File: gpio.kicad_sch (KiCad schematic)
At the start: 5 parts, among them J1 CONN_02X20, J2 CONN_02X20

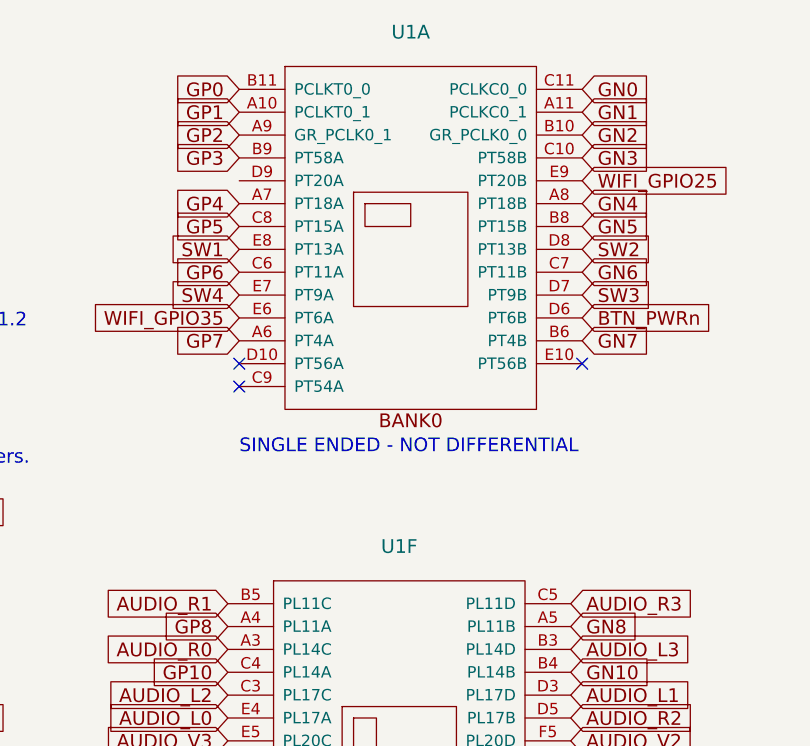
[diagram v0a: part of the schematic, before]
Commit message: Adding USB-C
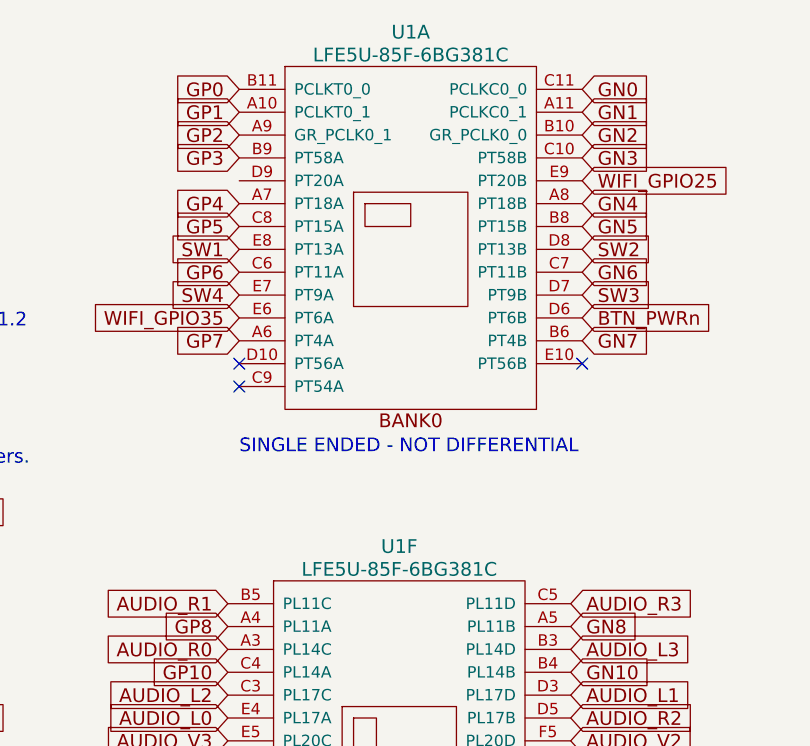
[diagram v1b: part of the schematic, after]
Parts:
- U1: value (none) -> LFE5U-85F-6BG381C; footprint (none) -> lfe5bg381:BGA-381_pitch0.8mm_dia0.4mm
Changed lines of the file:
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@@
   (title_block
     (title "ULX3S")
-    (rev "1.0.2")
+    (date "2023-01-19")
+    (rev "3.1.8")
     (company "EMARD")
     (comment 1 "GPIO 2.54 mm connectors")
@@
       (effects (font (size 1.524 1.524)))
     )
-    (property "Value" "" (id 1) (at 125.73 41.91 0)
-      (effects (font (size 1.524 1.524)))
-    )
-    (property "Footprint" "" (id 2) (at 99.06 39.37 0)
+    (property "Value" "LFE5U-85F-6BG381C" (id 1) (at 125.73 41.91 0)
+      (effects (font (size 1.524 1.524)))
+    )
+    (property "Footprint" "lfe5bg381:BGA-381_pitch0.8mm_dia0.4mm" (id 2) (at 99.06 39.37 0)
       (effects (font (size 1.524 1.524)) hide)
     )
@@
       (effects (font (size 1.524 1.524)))
     )
-    (property "Value" "" (id 1) (at 124.46 99.06 0)
-      (effects (font (size 1.524 1.524)))
-    )
-    (property "Footprint" "" (id 2) (at 97.79 96.52 0)
+    (property "Value" "LFE5U-85F-6BG381C" (id 1) (at 124.46 99.06 0)
+      (effects (font (size 1.524 1.524)))
+    )
+    (property "Footprint" "lfe5bg381:BGA-381_pitch0.8mm_dia0.4mm" (id 2) (at 97.79 96.52 0)
       (effects (font (size 1.524 1.524)) hide)
     )
